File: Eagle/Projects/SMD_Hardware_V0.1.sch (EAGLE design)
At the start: 36 parts, among them IC1 LM386M-1, Q1 12 MHz (ATS12A)

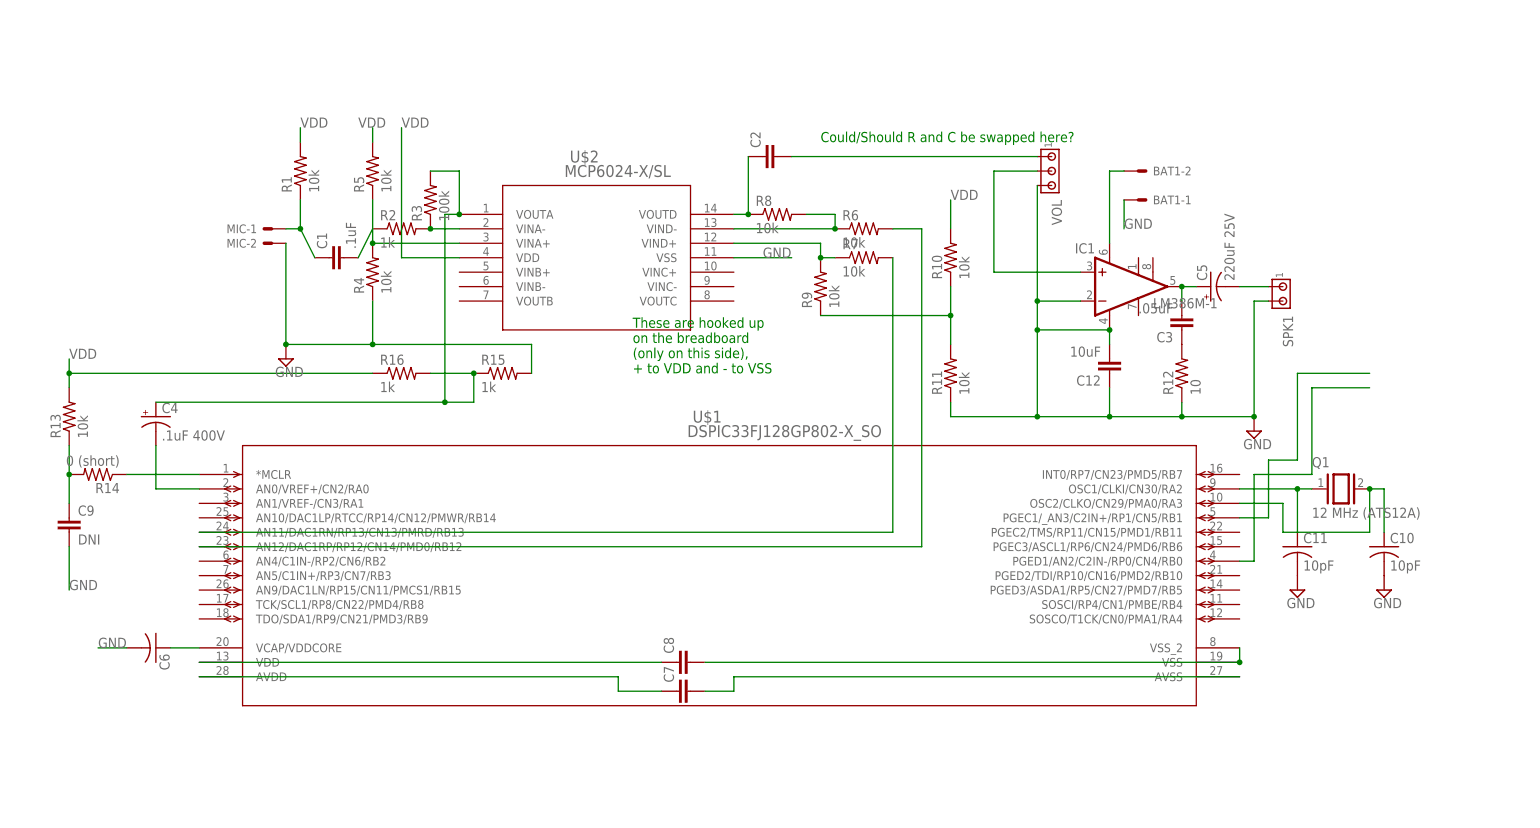
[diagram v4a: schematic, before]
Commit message: Cleaned up the schematic a bit and added an app note about anti-aliasing filters for ADC (which will need to be implemented)
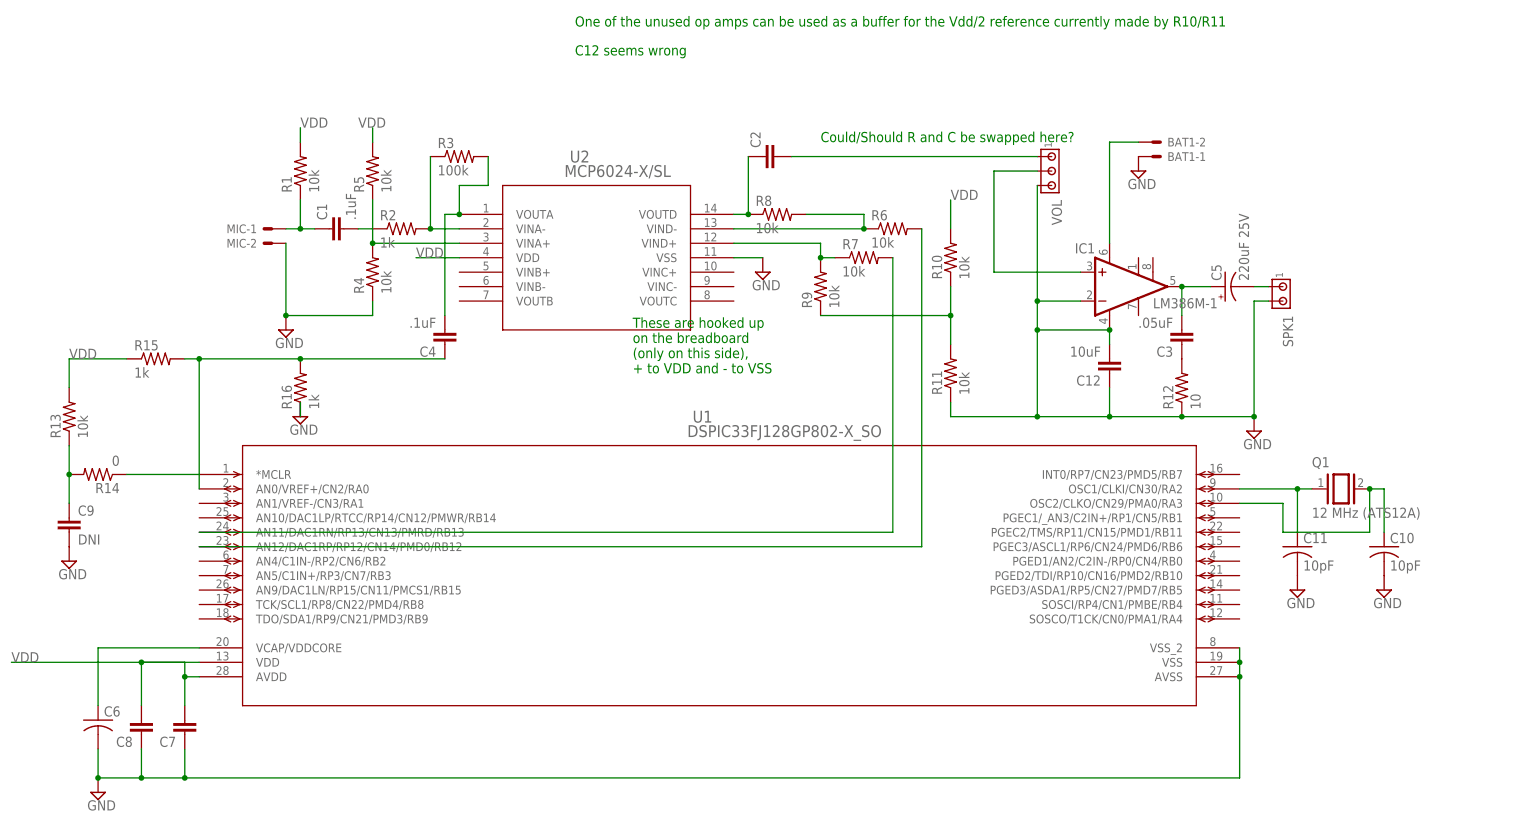
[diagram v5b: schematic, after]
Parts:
- C4: value .1uF 400V -> .1uF; device resistor:CPOL-US140CLH-0810 -> resistor:C-EUC0603
- R14: value 0 (short) -> 0
- renumbered U$1 to U1, U$2 to U2
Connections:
- removed net N$20: C8.2, U1.VSS, U1.VSS_2
- removed net N$26: C4.+, R15.1, R16.2, R3.2, U2.VOUTA
- removed net N$27: U1.PGED1/AN2/C2IN-/RP0/CN4/RB0
- removed net N$6: U1.PGEC1/_AN3/C2IN+/RP1/CN5/RB1
- new net N$30: C7.2, C8.2, U1.AVDD, U1.VDD
- net GND: now also C7.1, C8.1, R16.1, U1.AVSS, U1.VSS, U1.VSS_2; no longer R15.2
- net N$12: now also C4.1, R15.2, R16.2; no longer C4.-
- net N$19: now also U2.VDD; no longer C8.1, U1.VDD
- net N$21: now also R3.2, U2.VOUTA; no longer C7.1, U1.AVDD
- net N$22: now also C4.2; no longer C7.2, U1.AVSS
- net VDD: now also R15.1; no longer R16.1, U2.VDD
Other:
- note added: "C12 seems wrong"
- note added: "One of the unused op amps can be used as a buffer for the Vdd/2 reference currently made by R10/R11"
- moved on the sheet: BAT1-1, BAT1-2, C1, C3, C5, C6, C7, C8, R12, R15, R16, R3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
